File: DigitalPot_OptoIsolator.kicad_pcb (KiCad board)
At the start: 2 copper layers, 27.9 x 41.9 mm, 18 parts, among them J1 DIN-5, J2 5-Way Header, U1 TLP2361, U2 TLP2361, U3 TLP2361, U4 FODM8801

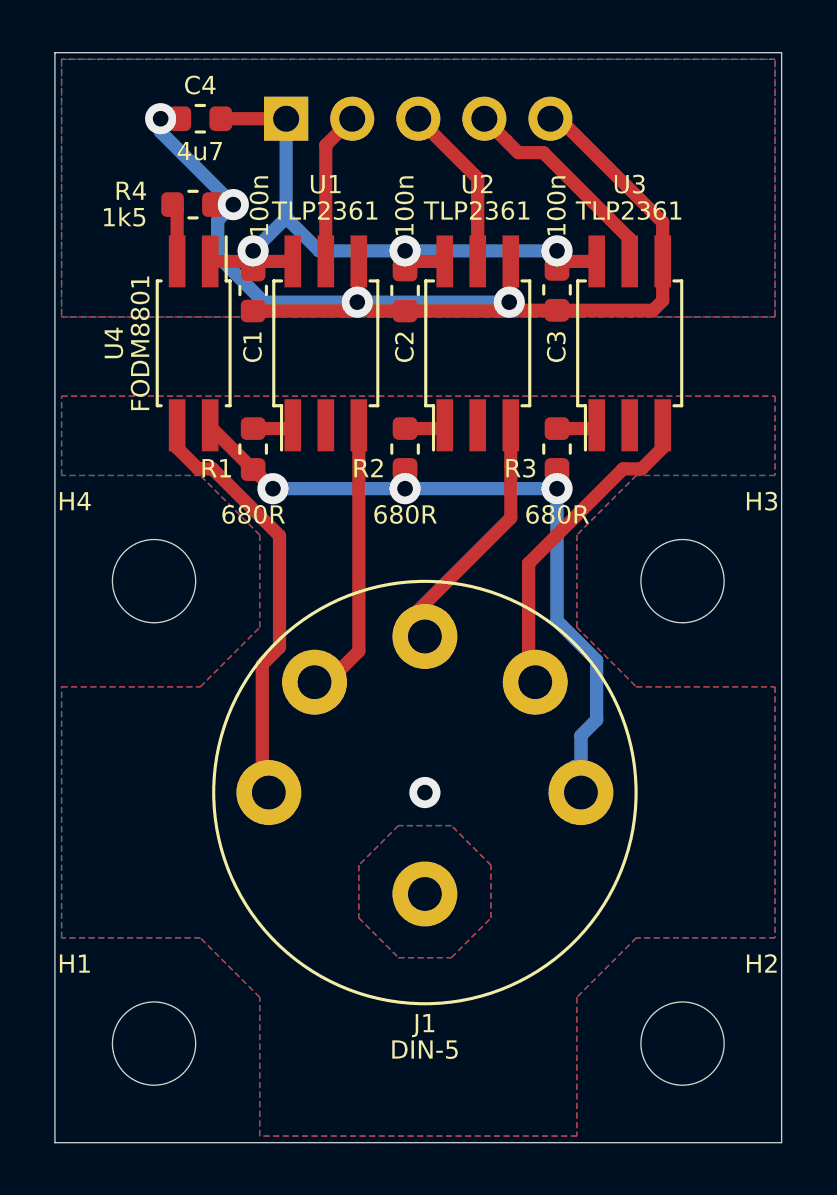
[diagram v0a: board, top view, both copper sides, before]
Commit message: Made board smaller to fit the box, removed two mounting screws, made central hole larger diameter so it can be used as a marking hole.
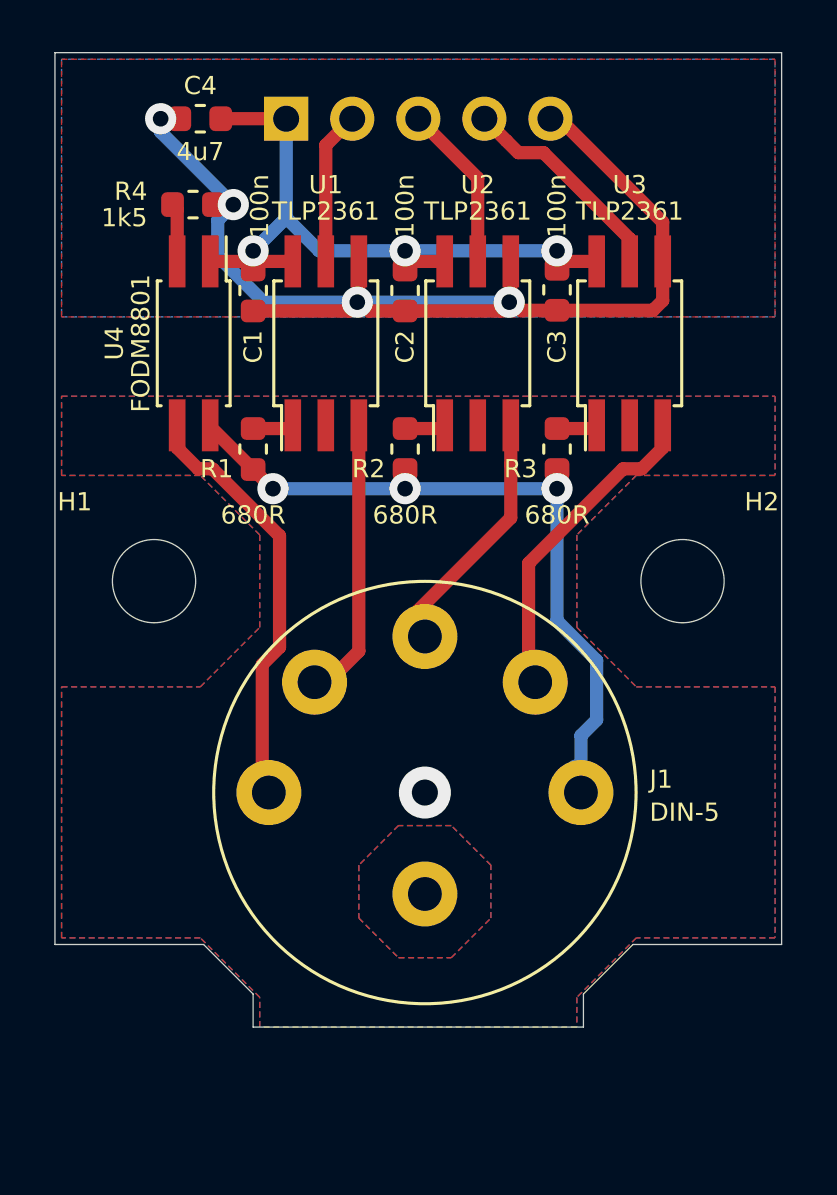
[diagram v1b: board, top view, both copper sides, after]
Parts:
- removed H3, H4: 3.2mm, MountingHole:MountingHole_3.2mm_M3
- moved H1 17.8 mm to (91.4, 38.1)
- moved H2 17.8 mm to (111.8, 38.1)
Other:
- board size 27.9 x 41.9 mm -> 27.9 x 37.5 mm
- board text added: "JAKUB NEDBAL DIGITAL POT OPTOISOLATOR v1.1 CC-BY 2019"
- board text removed: "JAKUB NEDBAL DIGITAL POT OPTOISOLATOR v1.0 CC-BY 2019"
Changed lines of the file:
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@@
-(kicad_pcb (version 20171130) (host pcbnew 5.1.2-f72e74a~84~ubuntu16.04.1)
+(kicad_pcb (version 20171130) (host pcbnew 5.1.3)
   (general
     (thickness 1.6)
-    (drawings 15)
+    (drawings 21)
     (tracks 104)
     (zones 0)
-    (modules 18)
+    (modules 16)
     (nets 15)
   )
@@
   (layers
     (0 F.Cu signal)
-    (31 B.Cu signal hide)
+    (31 B.Cu signal)
     (32 B.Adhes user)
     (33 F.Adhes user)
@@
     (add_net "Net-(R4-Pad1)")
   )
+  (module MountingHole:MountingHole_3.2mm_M3 (layer F.Cu)
+    (at 91.44 38.1)
+    (descr "Mounting Hole 3.2mm, no annular, M3")
+    (tags "mounting hole 3.2mm no annular m3")
+    (attr virtual)
+    (fp_text reference H1 (at -3.048 -3.048) (layer F.SilkS)
+      (effects (font (size 0.7 0.7) (thickness 0.11)))
+    )
+    (fp_text value 3.2mm (at 0 4.2) (layer F.Fab)
+      (effects (font (size 1 1) (thickness 0.15)))
+    )
+    (fp_circle (center 0 0) (end 3.45 0) (layer F.CrtYd) (width 0.05))
+    (fp_circle (center 0 0) (end 3.2 0) (layer Cmts.User) (width 0.15))
+    (fp_text user %R (at 0.3 0) (layer F.Fab)
+      (effects (font (size 1 1) (thickness 0.15)))
+    )
+    (pad 1 np_thru_hole circle (at 0 0) (size 3.2 3.2) (drill 3.2) (layers *.Cu *.Mask))
+  )
   (module jakub:DIN5 (layer F.Cu)
     (at 101.854 46.228)
     (descr "DIN 5 audio connector")
-    (fp_text reference J1 (at 0 8.89) (layer F.SilkS)
-      (effects (font (size 0.7 0.7) (thickness 0.11)))
-    )
-    (fp_text value DIN-5 (at 0 9.906) (layer F.SilkS)
-      (effects (font (size 0.7 0.7) (thickness 0.11)))
+    (fp_text reference J1 (at 8.636 -0.508) (layer F.SilkS)
+      (effects (font (size 0.7 0.7) (thickness 0.11)) (justify left))
+    )
+    (fp_text value DIN-5 (at 8.636 0.762) (layer F.SilkS)
+      (effects (font (size 0.7 0.7) (thickness 0.11)) (justify left))
     )
     (fp_circle (center 0 0) (end 0 8) (layer F.Fab) (width 0.1))
@@
   )
   (module MountingHole:MountingHole_3.2mm_M3 (layer F.Cu)
-    (at 91.44 38.1)
-    (descr "Mounting Hole 3.2mm, no annular, M3")
-    (tags "mounting hole 3.2mm no annular m3")
-    (attr virtual)
-    (fp_text reference H4 (at -3.048 -3.048) (layer F.SilkS)
-      (effects (font (size 0.7 0.7) (thickness 0.11)))
-    )
-    (fp_text value 3.2mm (at 0 4.2) (layer F.Fab)
-      (effects (font (size 1 1) (thickness 0.15)))
-    )
-    (fp_circle (center 0 0) (end 3.45 0) (layer F.CrtYd) (width 0.05))
-    (fp_circle (center 0 0) (end 3.2 0) (layer Cmts.User) (width 0.15))
-    (fp_text user %R (at 0.3 0) (layer F.Fab)
-      (effects (font (size 1 1) (thickness 0.15)))
-    )
-    (pad 1 np_thru_hole circle (at 0 0) (size 3.2 3.2) (drill 3.2) (layers *.Cu *.Mask))
-  )
-  (module MountingHole:MountingHole_3.2mm_M3 (layer F.Cu)
     (at 111.76 38.1)
     (descr "Mounting Hole 3.2mm, no annular, M3")
     (tags "mounting hole 3.2mm no annular m3")
     (attr virtual)
-    (fp_text reference H3 (at 3.048 -3.048) (layer F.SilkS)
-      (effects (font (size 0.7 0.7) (thickness 0.11)))
-    )
-    (fp_text value 3.2mm (at 0 4.2) (layer F.Fab)
-      (effects (font (size 1 1) (thickness 0.15)))
-    )
-    (fp_circle (center 0 0) (end 3.45 0) (layer F.CrtYd) (width 0.05))
-    (fp_circle (center 0 0) (end 3.2 0) (layer Cmts.User) (width 0.15))
-    (fp_text user %R (at 0.3 0) (layer F.Fab)
-      (effects (font (size 1 1) (thickness 0.15)))
-    )
-    (pad 1 np_thru_hole circle (at 0 0) (size 3.2 3.2) (drill 3.2) (layers *.Cu *.Mask))
-  )
-  (module MountingHole:MountingHole_3.2mm_M3 (layer F.Cu)
-    (at 111.76 55.88)
-    (descr "Mounting Hole 3.2mm, no annular, M3")
-    (tags "mounting hole 3.2mm no annular m3")
-    (attr virtual)
     (fp_text reference H2 (at 3.048 -3.048) (layer F.SilkS)
-      (effects (font (size 0.7 0.7) (thickness 0.11)))
-    )
-    (fp_text value 3.2mm (at 0 4.2) (layer F.Fab)
-      (effects (font (size 1 1) (thickness 0.15)))
-    )
-    (fp_circle (center 0 0) (end 3.45 0) (layer F.CrtYd) (width 0.05))
-    (fp_circle (center 0 0) (end 3.2 0) (layer Cmts.User) (width 0.15))
-    (fp_text user %R (at 0.3 0) (layer F.Fab)
-      (effects (font (size 1 1) (thickness 0.15)))
-    )
-    (pad 1 np_thru_hole circle (at 0 0) (size 3.2 3.2) (drill 3.2) (layers *.Cu *.Mask))
-  )
-  (module MountingHole:MountingHole_3.2mm_M3 (layer F.Cu)
-    (at 91.44 55.88)
-    (descr "Mounting Hole 3.2mm, no annular, M3")
-    (tags "mounting hole 3.2mm no annular m3")
-    (attr virtual)
-    (fp_text reference H1 (at -3.048 -3.048) (layer F.SilkS)
       (effects (font (size 0.7 0.7) (thickness 0.11)))
     )
@@
     )
   )
-  (gr_text "JAKUB NEDBAL\nDIGITAL POT OPTOISOLATOR v1.0\nCC-BY\n2019" (at 101.854 30.734) (layer B.SilkS)
+  (gr_line (start 95.25 55.245) (end 107.95 55.245) (layer Edge.Cuts) (width 0.05))
+  (gr_line (start 95.25 53.975) (end 95.25 55.245) (layer Edge.Cuts) (width 0.05))
+  (gr_line (start 93.345 52.07) (end 95.25 53.975) (layer Edge.Cuts) (width 0.05))
+  (gr_line (start 87.63 52.07) (end 93.345 52.07) (layer Edge.Cuts) (width 0.05))
+  (gr_line (start 107.95 53.975) (end 107.95 55.245) (layer Edge.Cuts) (width 0.05))
+  (gr_line (start 109.855 52.07) (end 107.95 53.975) (layer Edge.Cuts) (width 0.05))
+  (gr_line (start 115.57 52.07) (end 109.855 52.07) (layer Edge.Cuts) (width 0.05))
+  (gr_text "JAKUB NEDBAL\nDIGITAL POT OPTOISOLATOR v1.1\nCC-BY\n2019" (at 101.854 30.734) (layer B.SilkS)
     (effects (font (size 0.7 0.7) (thickness 0.11)) (justify mirror))
   )
@@
   )
   (gr_line (start 115.57 17.78) (end 87.63 17.78) (layer Edge.Cuts) (width 0.05))
-  (gr_line (start 115.57 59.69) (end 115.57 17.78) (layer Edge.Cuts) (width 0.05))
-  (gr_line (start 87.63 59.69) (end 115.57 59.69) (layer Edge.Cuts) (width 0.05))
-  (gr_line (start 87.63 17.78) (end 87.63 59.69) (layer Edge.Cuts) (width 0.05))
+  (gr_line (start 115.57 52.07) (end 115.57 17.78) (layer Edge.Cuts) (width 0.05))
+  (gr_line (start 87.63 17.78) (end 87.63 52.07) (layer Edge.Cuts) (width 0.05))
   (segment (start 94.9195 25.806) (end 95.25 26.1365) (width 0.508) (layer F.Cu) (net 1))
   (segment (start 93.599 25.806) (end 94.9195 25.806) (width 0.508) (layer F.Cu) (net 1))
@@
   (segment (start 110.998 32.973202) (end 110.189202 33.782) (width 0.508) (layer F.Cu) (net 4))
   (segment (start 110.998 32.106) (end 110.998 32.973202) (width 0.508) (layer F.Cu) (net 4))
-  (via (at 101.854 46.228) (size 1.2) (drill 0.6) (layers F.Cu B.Cu) (net 5))
+  (via (at 101.854 46.228) (size 2) (drill 1) (layers F.Cu B.Cu) (net 5))
   (segment (start 93.599 32.1565) (end 95.25 33.8075) (width 0.508) (layer F.Cu) (net 5))
   (segment (start 93.599 32.106) (end 93.599 32.1565) (width 0.508) (layer F.Cu) (net 5))
@@
       (pts
         (xy 115.316 34.036) (xy 109.982 34.036) (xy 107.696 36.322) (xy 107.696 39.878) (xy 109.982 42.164)
-        (xy 115.316 42.164) (xy 115.316 51.816) (xy 109.982 51.816) (xy 107.696 54.102) (xy 107.696 59.436)
-        (xy 95.504 59.436) (xy 95.504 54.102) (xy 93.218 51.816) (xy 87.884 51.816) (xy 87.884 42.164)
+        (xy 115.316 42.164) (xy 115.316 51.816) (xy 109.982 51.816) (xy 107.696 54.102) (xy 107.696 55.245)
+        (xy 95.504 55.245) (xy 95.504 54.102) (xy 93.218 51.816) (xy 87.884 51.816) (xy 87.884 42.164)
         (xy 93.218 42.164) (xy 95.504 39.878) (xy 95.504 36.322) (xy 93.218 34.036) (xy 87.884 34.036)
         (xy 87.884 30.988) (xy 115.316 30.988)
@@
       (pts
         (xy 115.316 34.036) (xy 109.982 34.036) (xy 107.696 36.322) (xy 107.696 39.878) (xy 109.982 42.164)
-        (xy 115.316 42.164) (xy 115.316 51.816) (xy 109.982 51.816) (xy 107.696 54.102) (xy 107.696 59.436)
-        (xy 95.504 59.436) (xy 95.504 54.102) (xy 93.218 51.816) (xy 87.884 51.816) (xy 87.884 42.164)
+        (xy 115.316 42.164) (xy 115.316 51.816) (xy 109.982 51.816) (xy 107.696 54.102) (xy 107.696 55.245)
+        (xy 95.504 55.245) (xy 95.504 54.102) (xy 93.218 51.816) (xy 87.884 51.816) (xy 87.884 42.164)
         (xy 93.218 42.164) (xy 95.504 39.878) (xy 95.504 36.322) (xy 93.218 34.036) (xy 87.884 34.036)
         (xy 87.884 30.988) (xy 115.316 30.988)
